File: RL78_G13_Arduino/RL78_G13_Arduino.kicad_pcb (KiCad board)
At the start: 2 copper layers, 100 x 57 mm, 32 parts, among them J1 Power, J2 Misc IOs, J3 Analog, J4 Misc IOS, J5 Misc IOs, J6 Communication, P2 POWER_JACKPTH, P3 E2 Lite, U1 R5F100FLAFP, U2 BA17805FP2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

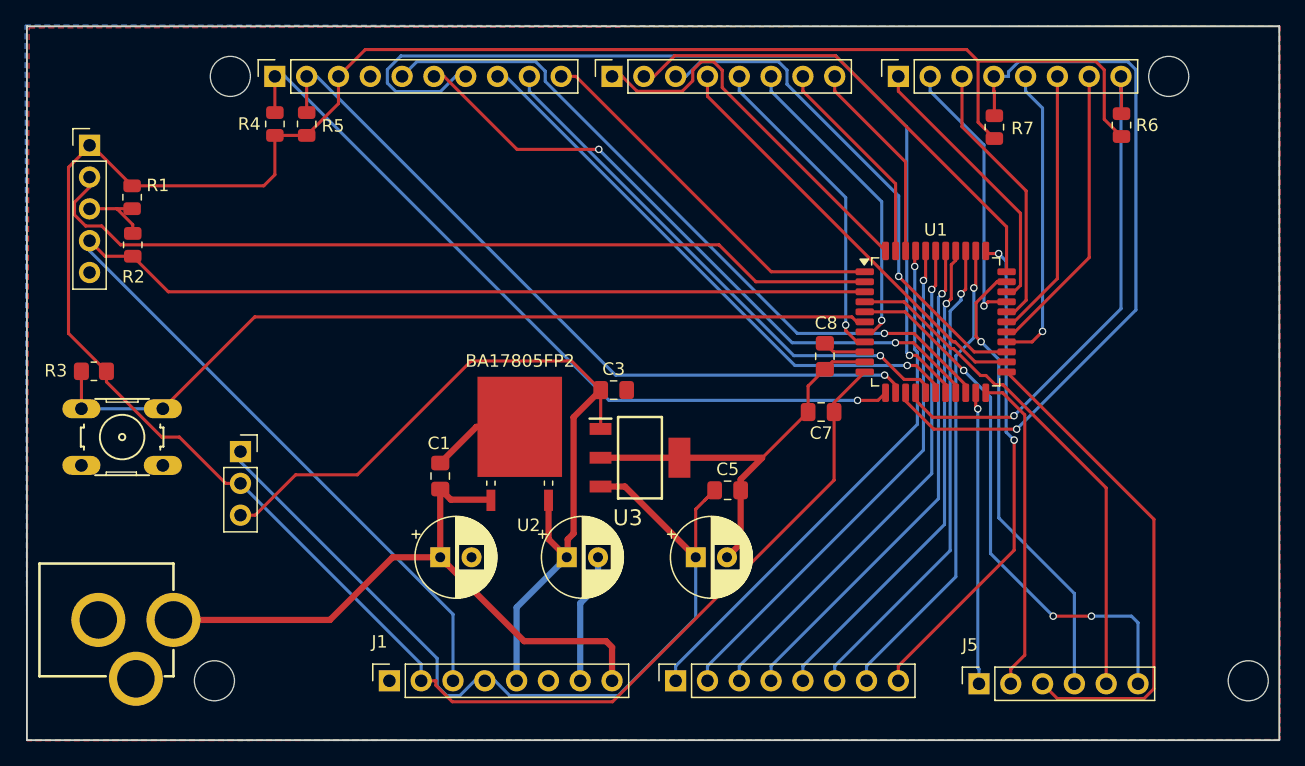
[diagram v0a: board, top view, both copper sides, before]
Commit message: Added a few other projects
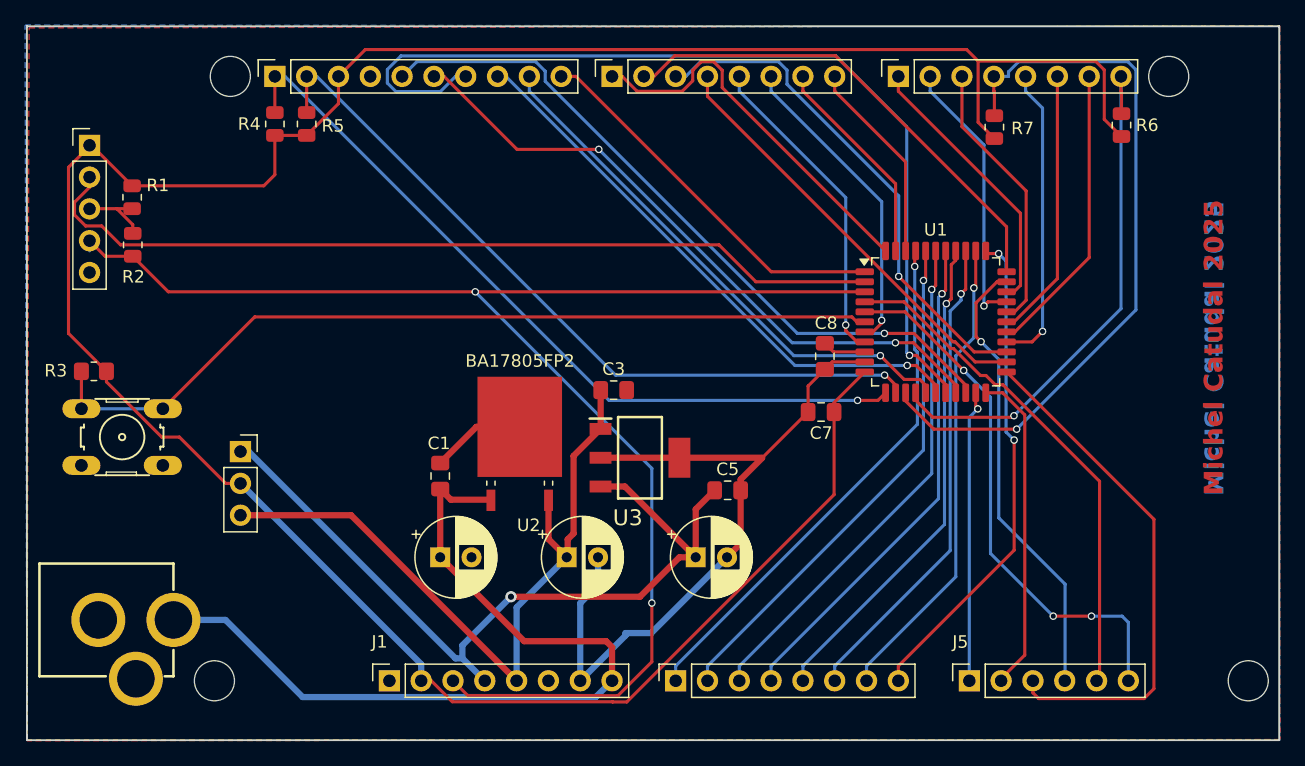
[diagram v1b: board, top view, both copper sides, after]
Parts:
- moved J5 0.81 mm to (125.2, 77.3)
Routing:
- net GND: track 55.0 -> 70.9 mm
- net /Vin: track 52.5 -> 67.2 mm
- net +5V: track 69.1 -> 58.7 mm
- net /~{RESET}: track 110.8 -> 117.3 mm, vias 0 -> 2
- net +3.3V: track 71.6 -> 65.6 mm, vias 0 -> 1
- net /MOSI_11: track 39.9 -> 41.3 mm
- net Net-(J5-Pin_6): track 44.3 -> 43.3 mm
- net /CS_11: track 36.8 -> 36.3 mm
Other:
- board text added: "Michel Catudal 2025"
